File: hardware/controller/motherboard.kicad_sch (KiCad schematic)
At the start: 49 parts, among them J10 TC2030, J2 Molex PicoBlade, J3 Conn_02x06_Odd_Even, J4 AFB10-S18LCA-00, J5 726386-2, J6 Conn_Coaxial_Small, J7 AFB10-S06LCA-00, J9 AFC11-S12ICA-00, Q1 PMZB350UPE,315, SW90 SW_Push, U1 NRF52840, U2 nPM1300-QEAA, Y1 32MHz, Y2 32.768 kHz

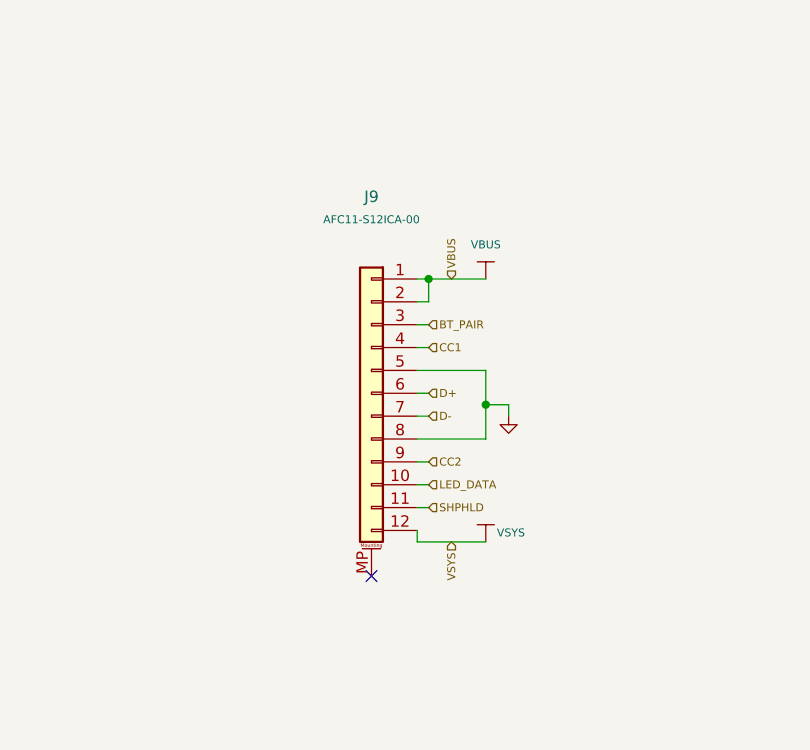
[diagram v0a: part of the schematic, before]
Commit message: feat(controller): 1x10 MB-DB header, isolate DB nets, drop DB buttons and LEDs
J9 (MB) and J8 (DB) as Conn_01x10 with I1 pinout; DB nets renamed DB_*,
no hierarchical links between MB and DB sheets; SW89, SW91, D4, D92 removed.
Layout around J9 still to be tidied.

Co-Authored-By: Claude Opus 5.5 (1M context) <noreply@anthropic.com>
Claude-Session: https://claude.ai/code/session_011u4PgyeeXFvTvHcxLBDiHw
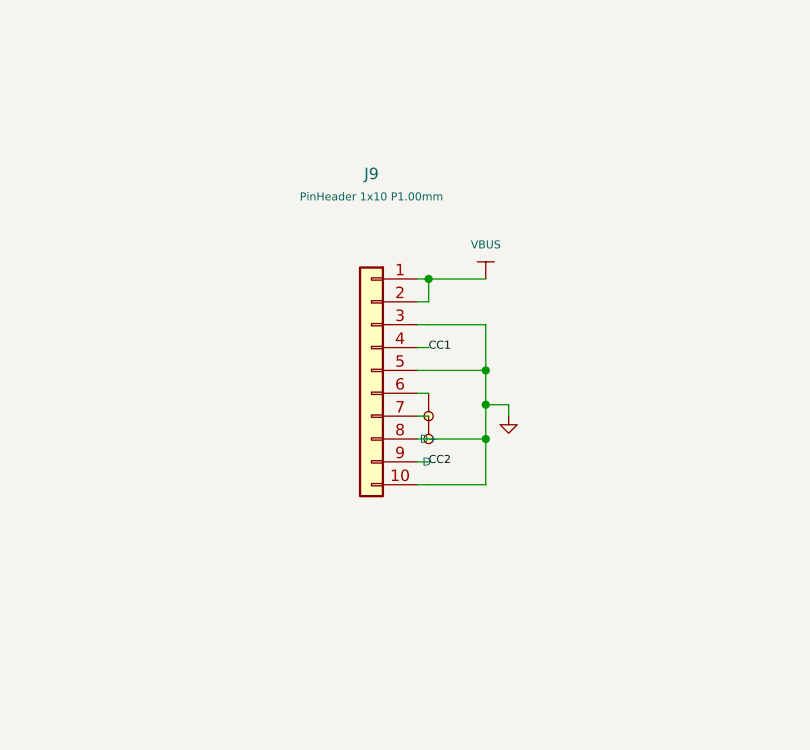
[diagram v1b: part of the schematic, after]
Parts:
- J9: value AFC11-S12ICA-00 -> PinHeader 1x10 P1.00mm; footprint easyeda2kicad:CONN-SMD-12P_AFC11-S12ICA-00 -> Connector_PinHeader_1.00mm:PinHeader_1x10_P1.00mm_Vertical; symbol Connector_Generic_MountingPin:Conn_01x12_MountingPin -> Connector_Generic:Conn_01x10; LCSC Part C262499 -> (none)
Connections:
- net BT_PAIR is gone; now on net GND: J9.3 (Pin_3)
- net LED_DATA is gone; now on net GND: J9.10 (Pin_10)
- net SHPHLD: no longer J9.11 (Pin_11)
- net VSYS: no longer J9.12 (Pin_12)
- no-connect marks 15 -> 14

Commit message: feat(controller): U2 on ibm_m nPM1300 symbol, PMIC step 1 (P1-P4, P7, P10)
BUCK2 drives VDD_NRF (L4 SW2-VOUT2, R10 470k on VSET2), BUCK1 terminated,
PVSS2 net-tie NT1 to GND, NTC to GND (TH1 removed), LSIN1 on VSYS,
VDDIO on VDD_NRF with C35 100n, GPIO0 PMIC_INT, GPIO1 LED_EN labels.

Co-Authored-By: Claude Opus 5.5 (1M context) <noreply@anthropic.com>
Claude-Session: https://claude.ai/code/session_011u4PgyeeXFvTvHcxLBDiHw
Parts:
- removed TH1: 10k, symbol Device:Thermistor_NTC
- added C34: 2.2u, symbol Device:C_Small
- added C35: 100n, symbol Device:C_Small
- added NT1: NetTie_2, symbol Device:NetTie_2
- BT1: footprint easyeda2kicad:LP803040 -> (none); LCSC Part - -> (none)
- C1, C17, C18, C2: footprint Capacitor_SMD:C_0402_1005Metric -> (none); LCSC Part C526985 -> (none)
- C10, C13, C22: footprint Capacitor_SMD:C_0402_1005Metric -> (none)
- C11: footprint Capacitor_SMD:C_0402_1005Metric -> (none); LCSC Part C106200 -> (none)
- C12, C5, C7, C8: footprint Capacitor_SMD:C_0402_1005Metric -> (none); LCSC Part C60474 -> (none)
- C14, C15, C27, C32, C33: footprint Capacitor_SMD:C_0603_1608Metric -> (none); LCSC Part C559769 -> (none)
- C16: footprint Capacitor_SMD:C_0402_1005Metric -> (none); LCSC Part C327054 -> (none)
- C20, C21, C6: footprint Capacitor_SMD:C_0603_1608Metric -> (none); LCSC Part C277476 -> (none)
- C28: footprint Capacitor_SMD:C_0603_1608Metric -> (none); LCSC Part C309478 -> (none)
- C29, C30, C31: footprint Capacitor_SMD:C_0603_1608Metric -> (none); LCSC Part C596327 -> (none)
- C3: footprint Capacitor_SMD:C_0402_1005Metric -> (none); LCSC Part C326068 -> (none)
- C4: footprint Capacitor_SMD:C_0402_1005Metric -> (none); LCSC Part C327230 -> (none)
- C9: footprint Capacitor_SMD:C_0402_1005Metric -> (none); LCSC Part C726612 -> (none)
- J2: footprint Connector_Molex:Molex_PicoBlade_53261-0271_1x02-1MP_P1.25mm_Horizontal -> easyeda2kicad:CONN-SMD_P2.00_S2B-PH-SM4-TB-LF-SN; LCSC Part C177225 -> C295747
- J3: now in the parts list
- J4: footprint easyeda2kicad:FPC-SMD_18P-P1.00_AFB10-S18LCA-00 -> (none); LCSC Part C7499267 -> (none); now in the parts list
- J6: footprint easyeda2kicad:IPEX-SMD_3P-L2.6-W2.6-LS3.0_ZCF-CF0001-0002IPEX -> (none)
- J7: footprint easyeda2kicad:FPC-SMD_6P-P1.00_AFB10-S6LCA-00 -> (none); LCSC Part C7499263 -> (none)
- J9: footprint Connector_PinHeader_1.00mm:PinHeader_1x10_P1.00mm_Vertical -> (none)
- L1: footprint Inductor_SMD:L_0402_1005Metric -> (none); LCSC Part C304335 -> (none)
- L2: footprint Inductor_SMD:L_0603_1608Metric_Pad1.05x0.95mm_HandSolder -> (none); LCSC Part C86083 -> (none)
- L3: footprint Inductor_SMD:L_0402_1005Metric -> (none); LCSC Part C381880 -> (none)
- L4: footprint Inductor_SMD:L_1008_2520Metric -> (none); symbol Device:L_Small -> Device:L; LCSC Part C5349606 -> (none)
- Q1: footprint easyeda2kicad:DFN1006-3 -> (none); LCSC Part C478140 -> (none)
- R10: footprint Resistor_SMD:R_0402_1005Metric -> (none); symbol Device:R_Small -> Device:R; LCSC Part C25792 -> (none)
- SW90: footprint easyeda2kicad:KEY-SMD_B3U-1000PM -> (none); LCSC Part C231329 -> (none)
- U1: footprint nrf52840_qiaa:AQFN50P700X700X85_HS-74N -> (none); LCSC Part C190794 -> (none)
- U2: symbol AltiumLib:root_0_nPM1300_QEAA_AltiumLib.DbLib -> ibm_m:nPM1300-QEAA; ALTIUM_VALUE nPM1300-QEAA -> (none); ARTIKKELNR NOCA N.A. -> (none); AUTHOR eisk -> (none); COMPONENT CLASS nRF_Devices -> (none); COMPONENT STATUS Active -> (none); COMPONENTLINK1DESCRIPTION Datasheet -> (none); COMPONENTLINK1URL N.A. -> (none); COMPONENTLINK2DESCRIPTION Supplier link -> (none); COMPONENTLINK2URL N.A. -> (none); FOOTPRINT DOC QFN-32 -> (none); HELPURL N.A. -> (none); LATESTREVISIONDATE 2022-11-14 -> (none); LCSC Part C7466043 -> (none); MANUFACTURER Nordic Semiconductor -> (none); MANUFACTURER PART NUMBER nPM1300-QEAA -> (none); NOTE N.A. -> (none); PAD COUNT 33 -> (none); PART NUMBER nPM1300-QEAA -> (none); PART NUMBER IPS N.A. -> (none); PART NUMBER NEMS 102000252 -> (none); PART NUMBER NORAUTRON N.A. -> (none); PARTID 102000252 -> (none); PUBLISHED 2022-02-17 -> (none); SUPPLIER 1 Nordic Semiconductor -> (none); SUPPLIER 2 N.A. -> (none); SUPPLIER PART NUMBER 1 nPM1300-QEAA -> (none); SUPPLIER PART NUMBER 2 N.A. -> (none)
- Y1: footprint easyeda2kicad:Crystal_SMD_2016-4Pin_2.0x1.6mm -> (none); LCSC Part C255896 -> (none)
- Y2: footprint easyeda2kicad:Crystal_SMD_3215-2Pin -> (none); LCSC Part C99010 -> (none)
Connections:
- net GND: now also Q1.G, U2.17 (VSET1), U2.18 (NTC), U2.2 (PVSS1), C35.2, NT1.1; no longer Q1.1 (G), U2.16 (VSET2), U2.6 (PVSS2)
- net VBAT: now also Q1.D; no longer Q1.3 (D)
- net VDD_NRF: now also L4.2, U2.12 (VDDIO), U2.32 (VOUT2), C35.1; no longer L4.1, U2.1 (VOUT1), U2.28 (LSIN1/VINLDO1)
- net VSYS: now also U2.1 (VOUT1), U2.28 (LSIN1); no longer U2.32 (VOUT2)
- net at R10.1: now also U2.16 (VSET2); no longer U2.17 (VSET1)
- net at J2.1: now also Q1.S; no longer Q1.2 (S)
- net at U2.3 (SW1): no longer L4.2
- net at U2.5 (SW2): now also L4.1
- net PMIC_INT: now reaches U2.7 (GPIO0)
- net LED_EN: now reaches U2.8 (GPIO1)
- net PVSS1 renamed PVSS2
- net PVSS2: now also U2.6 (PVSS2), NT1.2; no longer U2.2 (PVSS1)
- no-connect marks 14 -> 11
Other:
- note added: "Via to GND-layer on PVSS2"
- note removed: "Via to GND-layer on PVSS1"
- moved on the sheet: C27, C28, C29, C30, C31, C32, C33, L4, R10

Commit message: fix(controller): restore footprints and LCSC fields lost on symbol update; PMIC P5, S2, P8, P9
Footprint and LCSC Part restored from 6fba3e8 for every symbol whose value
is unchanged (MB and DB); J8/J9 descriptions restored. Q1 (now AO3401A)
left for manual footprint assignment.

Co-Authored-By: Claude Opus 5.5 (1M context) <noreply@anthropic.com>
Claude-Session: https://claude.ai/code/session_011u4PgyeeXFvTvHcxLBDiHw
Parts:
- added R11, R12: 4.7k, symbol Device:R
- added TP1: TestPoint, symbol Connector:TestPoint
- BT1: footprint (none) -> easyeda2kicad:LP803040; LCSC Part (none) -> -
- C1, C17, C18, C2: footprint (none) -> Capacitor_SMD:C_0402_1005Metric; LCSC Part (none) -> C526985
- C10, C13, C22: footprint (none) -> Capacitor_SMD:C_0402_1005Metric
- C11: footprint (none) -> Capacitor_SMD:C_0402_1005Metric; LCSC Part (none) -> C106200
- C12, C5, C7, C8: footprint (none) -> Capacitor_SMD:C_0402_1005Metric; LCSC Part (none) -> C60474
- C14, C15, C27, C32, C33: footprint (none) -> Capacitor_SMD:C_0603_1608Metric; LCSC Part (none) -> C559769
- C16: footprint (none) -> Capacitor_SMD:C_0402_1005Metric; LCSC Part (none) -> C327054
- C20, C21, C6: footprint (none) -> Capacitor_SMD:C_0603_1608Metric; LCSC Part (none) -> C277476
- C28: footprint (none) -> Capacitor_SMD:C_0603_1608Metric; LCSC Part (none) -> C309478
- C29, C30, C31: footprint (none) -> Capacitor_SMD:C_0603_1608Metric; LCSC Part (none) -> C596327
- C3: footprint (none) -> Capacitor_SMD:C_0402_1005Metric; LCSC Part (none) -> C326068
- C4: footprint (none) -> Capacitor_SMD:C_0402_1005Metric; LCSC Part (none) -> C327230
- C9: footprint (none) -> Capacitor_SMD:C_0402_1005Metric; LCSC Part (none) -> C726612
- J4: footprint (none) -> easyeda2kicad:FPC-SMD_18P-P1.00_AFB10-S18LCA-00; LCSC Part (none) -> C7499267
- J6: footprint (none) -> easyeda2kicad:IPEX-SMD_3P-L2.6-W2.6-LS3.0_ZCF-CF0001-0002IPEX
- J7: footprint (none) -> easyeda2kicad:FPC-SMD_6P-P1.00_AFB10-S6LCA-00; LCSC Part (none) -> C7499263
- J9: footprint (none) -> Connector_PinHeader_1.00mm:PinHeader_1x10_P1.00mm_Vertical
- L1: footprint (none) -> Inductor_SMD:L_0402_1005Metric; LCSC Part (none) -> C304335
- L2: footprint (none) -> Inductor_SMD:L_0603_1608Metric_Pad1.05x0.95mm_HandSolder; LCSC Part (none) -> C86083
- L3: footprint (none) -> Inductor_SMD:L_0402_1005Metric; LCSC Part (none) -> C381880
- L4: footprint (none) -> Inductor_SMD:L_1008_2520Metric; LCSC Part (none) -> C5349606
- Q1: value PMZB350UPE,315 -> AO3401A
- R10: footprint (none) -> Resistor_SMD:R_0402_1005Metric; LCSC Part (none) -> C25792
- SW90: footprint (none) -> easyeda2kicad:KEY-SMD_B3U-1000PM; LCSC Part (none) -> C231329
- U1: footprint (none) -> nrf52840_qiaa:AQFN50P700X700X85_HS-74N; LCSC Part (none) -> C190794
- U2: LCSC Part (none) -> C7466043
- Y1: footprint (none) -> easyeda2kicad:Crystal_SMD_2016-4Pin_2.0x1.6mm; LCSC Part (none) -> C255896
- Y2: footprint (none) -> easyeda2kicad:Crystal_SMD_3215-2Pin; LCSC Part (none) -> C99010
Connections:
- net SCL: now also R12.2
- net SDA: now also R11.2
- net SHPHLD: now also TP1.1
- net VBAT: now also Q1.S; no longer Q1.D
- net VDD_NRF: now also R11.1, R12.1
- net at J2.1: now also Q1.D; no longer Q1.S
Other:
- moved on the sheet: C35, U2

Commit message: feat(controller): Q1 as Transistor_FET:AO3401A (P9), unused parts moved off sheet
Co-Authored-By: Claude Opus 5.5 (1M context) <noreply@anthropic.com>
Claude-Session: https://claude.ai/code/session_011u4PgyeeXFvTvHcxLBDiHw
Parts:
- Q1: footprint (none) -> Package_TO_SOT_SMD:SOT-23; symbol Device:Q_PMOS -> Transistor_FET:AO3401A
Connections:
- net GND: now also Q1.1 (G); no longer Q1.G
- net VBAT: now also Q1.2 (S); no longer Q1.S
- net at J2.1: now also Q1.3 (D); no longer Q1.D
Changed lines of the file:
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@@
 	)
 	(symbol
-		(lib_id "Device:Q_PMOS")
+		(lib_id "Transistor_FET:AO3401A")
 		(at 49.53 185.42 0)
 		(mirror x)
@@
 			)
 		)
-		(property "Footprint" ""
-			(at 54.61 187.96 0)
+		(property "Footprint" "Package_TO_SOT_SMD:SOT-23"
+			(at 54.61 183.515 0)
+			(hide yes)
+			(show_name no)
+			(do_not_autoplace no)
+			(effects
+				(font
+					(size 1.27 1.27)
+					(italic yes)
+				)
+				(justify left)
+			)
+		)
+		(property "Datasheet" "http://www.aosmd.com/pdfs/datasheet/AO3401A.pdf"
+			(at 54.61 181.61 0)
 			(hide yes)
 			(show_name no)
@@
 					(size 1.27 1.27)
 				)
+				(justify left)
 			)
 		)
-		(property "Datasheet" ""
+		(property "Description" "-4.0A Id, -30V Vds, P-Channel MOSFET, SOT-23"
 			(at 49.53 185.42 0)
 			(hide yes)
@@
 			)
 		)
-		(property "Description" "P-MOSFET transistor"
-			(at 49.53 185.42 0)
-			(hide yes)
-			(show_name no)
-			(do_not_autoplace no)
-			(effects
-				(font
-					(size 1.27 1.27)
-				)
-			)
+		(pin "3"
 		)
-		(pin "S"
+		(pin "2"
 		)
-		(pin "D"
-		)
-		(pin "G"
+		(pin "1"
 		)
 		(instances
